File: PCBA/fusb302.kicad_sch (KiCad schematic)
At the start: 3 parts, among them U301 FUSB302B

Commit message: molex model
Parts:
- renumbered C301 to C401, C302 to C402, U301 to U401
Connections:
- net CC1: now also U401.1 (CC2), U401.14 (CC2); no longer U401.10 (CC1), U401.11 (CC1)
- net CC2: now also U401.10 (CC1), U401.11 (CC1); no longer U401.1 (CC2), U401.14 (CC2)
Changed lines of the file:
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@@
     (effects (font (size 1.27 1.27)) (justify left bottom))
   )
-  (hierarchical_label "CC2" (shape input) (at 143.51 88.9 0)
+  (hierarchical_label "CC2" (shape input) (at 143.51 86.36 0)
     (effects (font (size 1.27 1.27)) (justify left))
   )
-  (hierarchical_label "CC1" (shape input) (at 143.51 86.36 0)
+  (hierarchical_label "CC1" (shape input) (at 143.51 88.9 0)
     (effects (font (size 1.27 1.27)) (justify left))
   )
@@
   (symbol (lib_id "Device:C") (at 88.9 85.09 0)
     (in_bom yes) (on_board yes) (fields_autoplaced)
-    (property "Reference" "C301" (id 0) (at 92.71 83.8199 0)
+    (property "Reference" "C401" (id 0) (at 92.71 83.8199 0)
       (effects (font (size 1.27 1.27)) (justify left))
     )
@@
   (symbol (lib_id "power:GND") (at 101.6 88.9 0)
     (in_bom yes) (on_board yes) (fields_autoplaced)
-    (property "Reference" "#PWR0110" (id 0) (at 101.6 95.25 0)
+    (property "Reference" "#PWR0124" (id 0) (at 101.6 95.25 0)
       (effects (font (size 1.27 1.27)) hide)
     )
@@
   (symbol (lib_id "power:VDD") (at 88.9 81.28 0)
     (in_bom yes) (on_board yes) (fields_autoplaced)
-    (property "Reference" "#PWR0111" (id 0) (at 88.9 85.09 0)
+    (property "Reference" "#PWR0126" (id 0) (at 88.9 85.09 0)
       (effects (font (size 1.27 1.27)) hide)
     )
@@
   (symbol (lib_id "power:GND") (at 88.9 88.9 0)
     (in_bom yes) (on_board yes) (fields_autoplaced)
-    (property "Reference" "#PWR0112" (id 0) (at 88.9 95.25 0)
+    (property "Reference" "#PWR0125" (id 0) (at 88.9 95.25 0)
       (effects (font (size 1.27 1.27)) hide)
     )
@@
   (symbol (lib_id "power:GND") (at 130.81 96.52 0)
     (in_bom yes) (on_board yes) (fields_autoplaced)
-    (property "Reference" "#PWR0109" (id 0) (at 130.81 102.87 0)
+    (property "Reference" "#PWR0122" (id 0) (at 130.81 102.87 0)
       (effects (font (size 1.27 1.27)) hide)
     )
@@
   (symbol (lib_id "Device:C") (at 101.6 85.09 0)
     (in_bom yes) (on_board yes) (fields_autoplaced)
-    (property "Reference" "C302" (id 0) (at 105.41 83.8199 0)
+    (property "Reference" "C402" (id 0) (at 105.41 83.8199 0)
       (effects (font (size 1.27 1.27)) (justify left))
     )
@@
   (symbol (lib_id "power:VDD") (at 128.27 76.2 0)
     (in_bom yes) (on_board yes) (fields_autoplaced)
-    (property "Reference" "#PWR0113" (id 0) (at 128.27 80.01 0)
+    (property "Reference" "#PWR0123" (id 0) (at 128.27 80.01 0)
       (effects (font (size 1.27 1.27)) hide)
     )
@@
   (symbol (lib_id "Interface_USB:FUSB302B01MPX") (at 130.81 86.36 0)
     (in_bom yes) (on_board yes) (fields_autoplaced)
-    (property "Reference" "U301" (id 0) (at 132.8294 96.52 0)
+    (property "Reference" "U401" (id 0) (at 132.8294 96.52 0)
       (effects (font (size 1.27 1.27)) (justify left))
     )

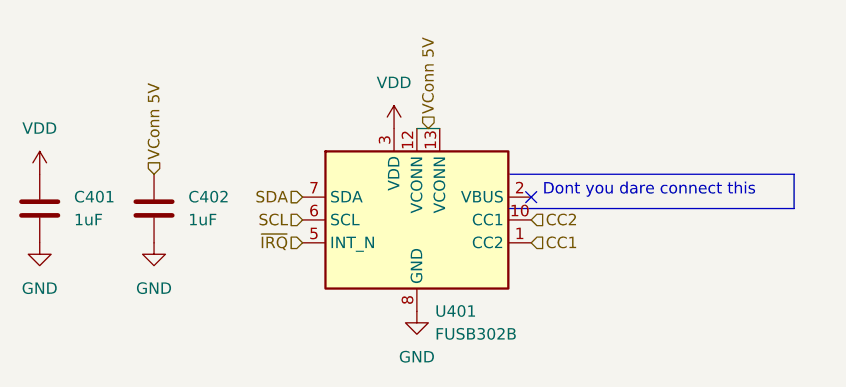
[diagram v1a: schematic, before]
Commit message: Jtag on usb-c
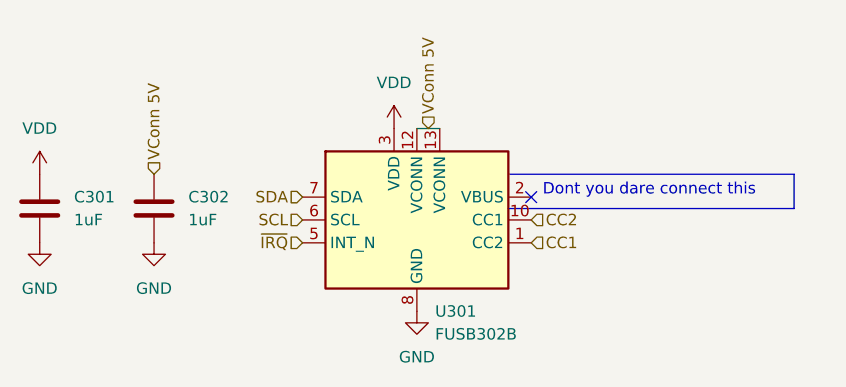
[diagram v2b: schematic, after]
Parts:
- renumbered C401 to C301, C402 to C302, U401 to U301
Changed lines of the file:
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@@
   (symbol (lib_id "Device:C") (at 88.9 85.09 0)
     (in_bom yes) (on_board yes) (fields_autoplaced)
-    (property "Reference" "C401" (id 0) (at 92.71 83.8199 0)
+    (property "Reference" "C301" (id 0) (at 92.71 83.8199 0)
       (effects (font (size 1.27 1.27)) (justify left))
     )
@@
   (symbol (lib_id "Device:C") (at 101.6 85.09 0)
     (in_bom yes) (on_board yes) (fields_autoplaced)
-    (property "Reference" "C402" (id 0) (at 105.41 83.8199 0)
+    (property "Reference" "C302" (id 0) (at 105.41 83.8199 0)
       (effects (font (size 1.27 1.27)) (justify left))
     )
@@
   (symbol (lib_id "Interface_USB:FUSB302B01MPX") (at 130.81 86.36 0)
     (in_bom yes) (on_board yes) (fields_autoplaced)
-    (property "Reference" "U401" (id 0) (at 132.8294 96.52 0)
+    (property "Reference" "U301" (id 0) (at 132.8294 96.52 0)
       (effects (font (size 1.27 1.27)) (justify left))
     )

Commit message: Finish routing
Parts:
- renumbered C301 to C401, C302 to C402, U301 to U401
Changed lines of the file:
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@@
   (symbol (lib_id "Device:C") (at 88.9 85.09 0)
     (in_bom yes) (on_board yes) (fields_autoplaced)
-    (property "Reference" "C301" (id 0) (at 92.71 83.8199 0)
+    (property "Reference" "C401" (id 0) (at 92.71 83.8199 0)
       (effects (font (size 1.27 1.27)) (justify left))
     )
@@
   (symbol (lib_id "Device:C") (at 101.6 85.09 0)
     (in_bom yes) (on_board yes) (fields_autoplaced)
-    (property "Reference" "C302" (id 0) (at 105.41 83.8199 0)
+    (property "Reference" "C402" (id 0) (at 105.41 83.8199 0)
       (effects (font (size 1.27 1.27)) (justify left))
     )
@@
   (symbol (lib_id "Interface_USB:FUSB302B01MPX") (at 130.81 86.36 0)
     (in_bom yes) (on_board yes) (fields_autoplaced)
-    (property "Reference" "U301" (id 0) (at 132.8294 96.52 0)
+    (property "Reference" "U401" (id 0) (at 132.8294 96.52 0)
       (effects (font (size 1.27 1.27)) (justify left))
     )
